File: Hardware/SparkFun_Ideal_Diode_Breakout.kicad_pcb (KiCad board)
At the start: 4 copper layers, 12.7 x 15.2 mm, 35 parts, among them J1 Conn_01x05, J2 Conn_01x05, Q1 BCM857BS-7-F, Q2 DMG2305UX, Q3 BCM857BS-7-F, Q4 DMG2305UX, Q5 BCM857BS-7-F, Q6 DMG2305UX, Q7 BCM857BS-7-F, Q8 DMG2305UX

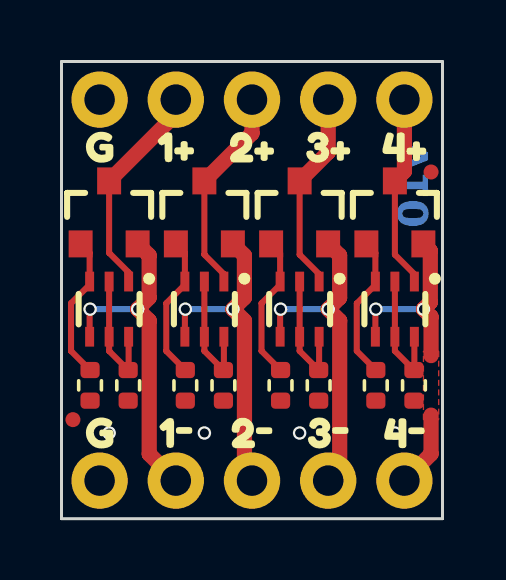
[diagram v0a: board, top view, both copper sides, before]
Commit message: Design review updates
Update page info on schematic and board
Separate schematic sections with lines and header text
Add power ratings
Add diode symbols to schematic
Change GND symbol silk to "G"
Check and exclude ERC and DRC errors
Change top silk to "INx" and "Ox"
Change GND silk to inverted text
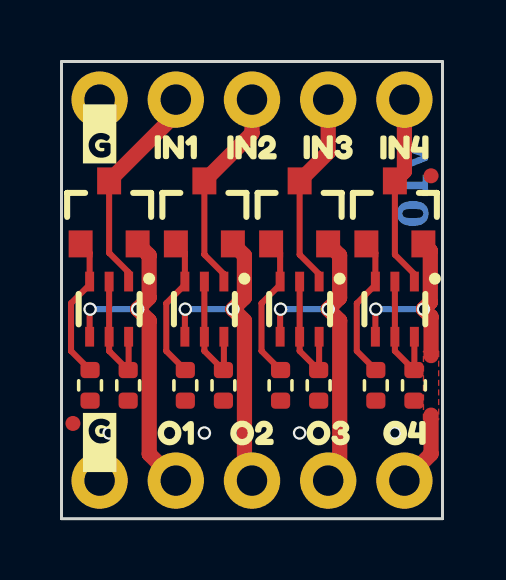
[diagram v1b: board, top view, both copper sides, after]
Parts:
- removed kibuzzard-6765BD62 (x2): G***, kibuzzard-6765BD62
- removed kibuzzard-6765BD93: G***, kibuzzard-6765BD93
- removed kibuzzard-6765BDA7: G***, kibuzzard-6765BDA7
- removed kibuzzard-6765BDAB: G***, kibuzzard-6765BDAB
- removed kibuzzard-6765BDB1: G***, kibuzzard-6765BDB1
- removed kibuzzard-6765BE3E: G***, kibuzzard-6765BE3E
- removed kibuzzard-6765BE43: G***, kibuzzard-6765BE43
- removed kibuzzard-6765BE4D: G***, kibuzzard-6765BE4D
- removed kibuzzard-6765BE51: G***, kibuzzard-6765BE51
- added kibuzzard-6765D0F5: G***, kibuzzard-6765D0F5, F.Cu at (119.4, 112.1)
- added kibuzzard-6765D0FB: G***, kibuzzard-6765D0FB, F.Cu at (121.9, 112.1)
- added kibuzzard-6765D145: G***, kibuzzard-6765D145, F.Cu at (124.5, 112.1)
- added kibuzzard-6765D14E: G***, kibuzzard-6765D14E, F.Cu at (127.0, 112.1)
- added kibuzzard-6765D154: G***, kibuzzard-6765D154, F.Cu at (119.4, 121.6)
- added kibuzzard-6765D159: G***, kibuzzard-6765D159, F.Cu at (121.9, 121.6)
- added kibuzzard-6765D15F: G***, kibuzzard-6765D15F, F.Cu at (124.5, 121.6)
- added kibuzzard-6765D166: G***, kibuzzard-6765D166, F.Cu at (127.0, 121.6)
- added kibuzzard-6765D25C: G***, kibuzzard-6765D25C, F.Cu at (116.8, 121.9)
- added kibuzzard-6765D25C: G***, kibuzzard-6765D25C, B.Cu at (116.8, 121.9)
- added kibuzzard-6765D292: G***, kibuzzard-6765D292, F.Cu at (116.8, 111.6)
- added kibuzzard-6765D292: G***, kibuzzard-6765D292, B.Cu at (116.8, 111.6)
- moved FID1 0.13 mm to (116.0, 121.3)
- moved FID4 0.13 mm to (127.9, 113.0)

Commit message: Change to 2 layer
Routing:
- removed copper zone on In1.Cu, net GND
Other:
- copper layers 4 -> 2
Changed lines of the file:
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@@
 	(layers
 		(0 "F.Cu" signal)
-		(1 "In1.Cu" signal)
-		(2 "In2.Cu" signal)
 		(31 "B.Cu" signal)
 		(34 "B.Paste" user)
@@
 			)
 			(layer "dielectric 1"
-				(type "prepreg")
-				(thickness 0.1)
-				(material "FR4")
-				(epsilon_r 4.5)
-				(loss_tangent 0.02)
-			)
-			(layer "In1.Cu"
-				(type "copper")
-				(thickness 0.035)
-			)
-			(layer "dielectric 2"
 				(type "core")
-				(thickness 1.24)
-				(material "FR4")
-				(epsilon_r 4.5)
-				(loss_tangent 0.02)
-			)
-			(layer "In2.Cu"
-				(type "copper")
-				(thickness 0.035)
-			)
-			(layer "dielectric 3"
-				(type "prepreg")
-				(thickness 0.1)
+				(thickness 1.51)
 				(material "FR4")
 				(epsilon_r 4.5)
@@
 				(font
 					(size 0.001 0.001)
+					(thickness 0.15)
 				)
 			)
@@
 				(font
 					(size 0.001 0.001)
+					(thickness 0.15)
 				)
 			)
@@
 		(tags "SparkFun")
 		(property "Reference" "J2"
-			(at 0 -1.397 360)
+			(at 0 -1.397 0)
 			(layer "F.Fab")
 			(effects
@@
 		)
 		(property "Value" "Conn_01x05"
-			(at 0 1.27 360)
+			(at 0 1.27 0)
 			(layer "F.Fab")
 			(effects
@@
 			(remove_unused_layers yes)
 			(keep_end_layers yes)
-			(zone_layer_connections "In1.Cu")
+			(zone_layer_connections)
 			(net 1 "GND")
 			(pinfunction "Pin_1")
@@
 				(font
 					(size 0.001 0.001)
+					(thickness 0.15)
 				)
 			)
@@
 				(font
 					(size 0.001 0.001)
+					(thickness 0.15)
 				)
 			)
@@
 				(font
 					(size 0.001 0.001)
+					(thickness 0.15)
 				)
 			)
@@
 				(font
 					(size 0.001 0.001)
+					(thickness 0.15)
 				)
 			)
@@
 				(font
 					(size 0.001 0.001)
+					(thickness 0.15)
 				)
 			)
@@
 				(font
 					(size 0.001 0.001)
+					(thickness 0.15)
 				)
 			)
@@
 				(font
 					(size 0.001 0.001)
+					(thickness 0.15)
 				)
 			)
@@
 				(font
 					(size 0.001 0.001)
+					(thickness 0.15)
 				)
 			)
@@
 				(font
 					(size 0.001 0.001)
+					(thickness 0.15)
 				)
 			)
@@
 				(font
 					(size 0.001 0.001)
+					(thickness 0.15)
 				)
 			)
@@
 				(font
 					(size 0.001 0.001)
+					(thickness 0.15)
 				)
 			)
@@
 				(font
 					(size 0.001 0.001)
+					(thickness 0.15)
 				)
 			)
@@
 		(tags "SparkFun")
 		(property "Reference" "J1"
-			(at 0 -1.397 360)
+			(at 0 -1.397 0)
 			(layer "F.Fab")
 			(effects
@@
 		)
 		(property "Value" "Conn_01x05"
-			(at 0 1.27 360)
+			(at 0 1.27 0)
 			(layer "F.Fab")
 			(effects
@@
 			(remove_unused_layers yes)
 			(keep_end_layers yes)
-			(zone_layer_connections "In1.Cu")
+			(zone_layer_connections)
 			(net 1 "GND")
 			(pinfunction "Pin_1")
@@
 				(font
 					(size 0.001 0.001)
+					(thickness 0.15)
 				)
 			)
@@
 				(font
 					(size 0.001 0.001)
+					(thickness 0.15)
 				)
 			)
@@
 				(font
 					(size 0.001 0.001)
+					(thickness 0.15)
 				)
 			)
@@
 				(font
 					(size 0.001 0.001)
+					(thickness 0.15)
 				)
 			)
@@
 				(font
 					(size 0.001 0.001)
+					(thickness 0.15)
 				)
 			)
@@
 				(font
 					(size 0.001 0.001)
+					(thickness 0.15)
 				)
 			)
@@
 		(tags "SparkFun Logo")
 		(property "Reference" "G***"
-			(at 0 2 360)
+			(at 0 2 0)
 			(layer "B.Fab")
 			(hide yes)
@@
 		)
 		(property "Value" "Flame"
-			(at 0 -2 360)
+			(at 0 -2 0)
 			(layer "B.Fab")
 			(hide yes)
@@
 		(tags "SparkFun Open Source Hardware Gear")
 		(property "Reference" "Ref**"
-			(at 0 2 360)
+			(at 0 2 0)
 			(layer "B.Fab")
 			(hide yes)
@@
 		)
 		(property "Value" "Val**"
-			(at 0 -1.6 360)
+			(at 0 -1.6 0)
 			(layer "B.Fab")
 			(hide yes)
@@
 		(tags "kb_params=eyJBbGlnbm1lbnRDaG9pY2UiOiAiTGVmdCIsICJDYXBMZWZ0Q2hvaWNlIjogIiIsICJDYXBSaWdodENob2ljZSI6ICIiLCAiRm9udENvbWJvQm94IjogIkZyZWRkeVNwYXJrLVJlZ3VsYXIiLCAiSGVpZ2h0Q3RybCI6IDIuMCwgIkxheWVyQ29tYm9Cb3giOiAiRi5TaWxrUyIsICJMaW5lU3BhY2luZ0N0cmwiOiAxLjUsICJNdWx0aUxpbmVUZXh0IjogIklkZWFsIiwgIlBhZGRpbmdCb3R0b21DdHJsIjogMC4wLCAiUGFkZGluZ0xlZnRDdHJsIjogMC4wLCAiUGFkZGluZ1JpZ2h0Q3RybCI6IDAuMCwgIlBhZGRpbmdUb3BDdHJsIjogMC4wLCAiV2lkdGhDdHJsIjogMC4wLCAiYWR2YW5jZWRDaGVja2JveCI6IGZhbHNlLCAiaW5saW5lRm9ybWF0VGV4dGJveCI6IGZhbHNlLCAibGluZW92ZXJTdHlsZUNob2ljZSI6ICJTcXVhcmUiLCAibGluZW92ZXJUaGlja25lc3NDdHJsIjogMX0=")
 		(property "Reference" "kibuzzard-6765BB94"
-			(at 0 4.120961 360)
+			(at 0 4.120961 0)
 			(layer "B.SilkS")
 			(hide yes)
@@
 				(font
 					(size 0.001 0.001)
+					(thickness 0.15)
 				)
 				(justify mirror)
@@
 		)
 		(property "Value" "G***"
-			(at 0 -4.120961 360)
+			(at 0 -4.120961 0)
 			(layer "B.SilkS")
 			(hide yes)
@@
 				(font
 					(size 0.001 0.001)
+					(thickness 0.15)
 				)
 				(justify mirror)
@@
 		)
 		(property "Footprint" ""
-			(at 0 0 360)
+			(at 0 0 0)
 			(layer "B.Fab")
 			(hide yes)
@@
 		)
 		(property "Datasheet" ""
-			(at 0 0 360)
+			(at 0 0 0)
 			(layer "B.Fab")
 			(hide yes)
@@
 		)
 		(property "Description" ""
-			(at 0 0 360)
+			(at 0 0 0)
 			(layer "B.Fab")
 			(hide yes)
@@
 		(tags "kb_params=eyJBbGlnbm1lbnRDaG9pY2UiOiAiTGVmdCIsICJDYXBMZWZ0Q2hvaWNlIjogIiIsICJDYXBSaWdodENob2ljZSI6ICIiLCAiRm9udENvbWJvQm94IjogIkZyZWRkeVNwYXJrLVJlZ3VsYXIiLCAiSGVpZ2h0Q3RybCI6IDIuMCwgIkxheWVyQ29tYm9Cb3giOiAiRi5TaWxrUyIsICJMaW5lU3BhY2luZ0N0cmwiOiAxLjUsICJNdWx0aUxpbmVUZXh0IjogIkRpb2RlcyIsICJQYWRkaW5nQm90dG9tQ3RybCI6IDAuMCwgIlBhZGRpbmdMZWZ0Q3RybCI6IDAuMCwgIlBhZGRpbmdSaWdodEN0cmwiOiAwLjAsICJQYWRkaW5nVG9wQ3RybCI6IDAuMCwgIldpZHRoQ3RybCI6IDAuMCwgImFkdmFuY2VkQ2hlY2tib3giOiBmYWxzZSwgImlubGluZUZvcm1hdFRleHRib3giOiBmYWxzZSwgImxpbmVvdmVyU3R5bGVDaG9pY2UiOiAiU3F1YXJlIiwgImxpbmVvdmVyVGhpY2tuZXNzQ3RybCI6IDF9")
 		(property "Reference" "kibuzzard-6765BBA3"
-			(at 0 4.1181 360)
+			(at 0 4.1181 0)
 			(layer "B.SilkS")
 			(hide yes)
@@
 				(font
 					(size 0.001 0.001)
+					(thickness 0.15)
 				)
 				(justify mirror)
@@
 		)
 		(property "Value" "G***"
-			(at 0 -4.1181 360)
+			(at 0 -4.1181 0)
 			(layer "B.SilkS")
 			(hide yes)
@@
 				(font
 					(size 0.001 0.001)
+					(thickness 0.15)
 				)
 				(justify mirror)
@@
 		)
 		(property "Footprint" ""
-			(at 0 0 360)
+			(at 0 0 0)
 			(layer "B.Fab")
 			(hide yes)
@@
 		)
 		(property "Datasheet" ""
-			(at 0 0 360)
+			(at 0 0 0)
 			(layer "B.Fab")
 			(hide yes)
@@
 		)
 		(property "Description" ""
-			(at 0 0 360)
+			(at 0 0 0)
 			(layer "B.Fab")
 			(hide yes)
@@
 		(net 1)
 		(net_name "GND")
-		(layers "F.Cu" "In1.Cu" "B.Cu")
+		(layers "F&B.Cu")
 		(hatch edge 0.5)
 		(connect_pads
